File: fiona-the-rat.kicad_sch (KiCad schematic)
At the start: 54 parts, among them J1 XTAL_TP, J14 GND_TP_2, J15 GND_TP_3, J16 USB_TP_N, J17 USB_TP_P, J2 USB_C_Receptacle_PowerOnly_6P, J3 GND_TP_1, J4 VBAT_ADC_TP, J5 ~{CHG}_TP, J6 +1V1_TP, J7 VBAT_TP, J8 +3V3_TP, J9 SWD, SW1 1825027-8, U1 RP2040, U3 W25Q128JVSIQ, U4 BQ21040DBVR, U5 AP2112K-3.3, Y1 Crystal_GND24

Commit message: adding stuff
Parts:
- added J6: Periph, Connector_JST:JST_XH_B2B-XH-A_1x02_P2.50mm_Vertical, symbol Connector:Conn_01x02_Pin
- added MOSFET1: DMN3042L-7, DMN3042L-7-footprints:SOT23_DMN3042L_DIO, symbol 2025-07-08_15-36-45:DMN3042L-7
- added R6: 10K, Resistor_SMD:R_0603_1608Metric, symbol Device:R
- renumbered J17 to J1, J5 to J10, J6 to J11, J7 to J12, J8 to J13, J9 to J14, J16 to J2, J1 to J3, J2 to J4, J4 to J5, J3 to J7, J14 to J8, J15 to J9, R9 to R10, R6 to R7, R7 to R8, R8 to R9
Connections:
- net GND: now also MOSFET1.2 (S), R6.1
- net VBAT: now also J6.2 (Pin_2)
- net LEDs/DIN: now reaches U1.5 (GPIO3)
- net at U1.6 (GPIO4): now also MOSFET1.1 (G), R6.2
- new net: J6.1 (Pin_1), MOSFET1.3 (D)
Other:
- added sheet LEDs (LEDs.kicad_sch)

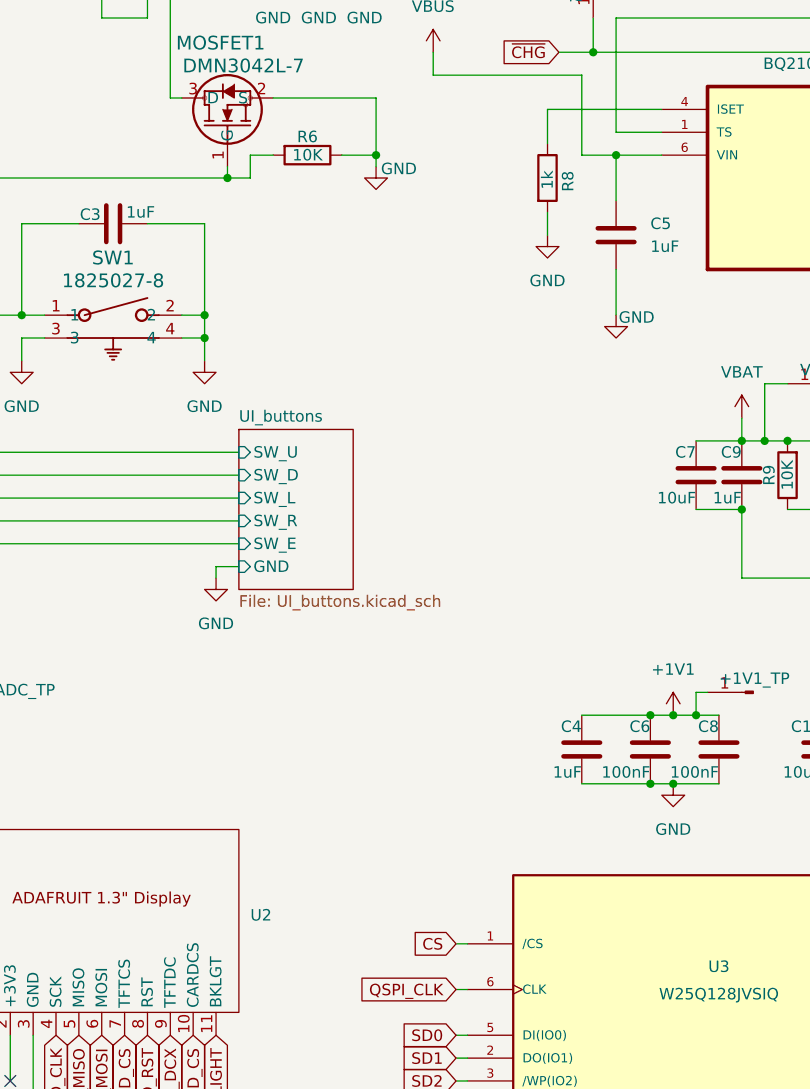
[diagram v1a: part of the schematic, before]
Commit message: changed lib to owned
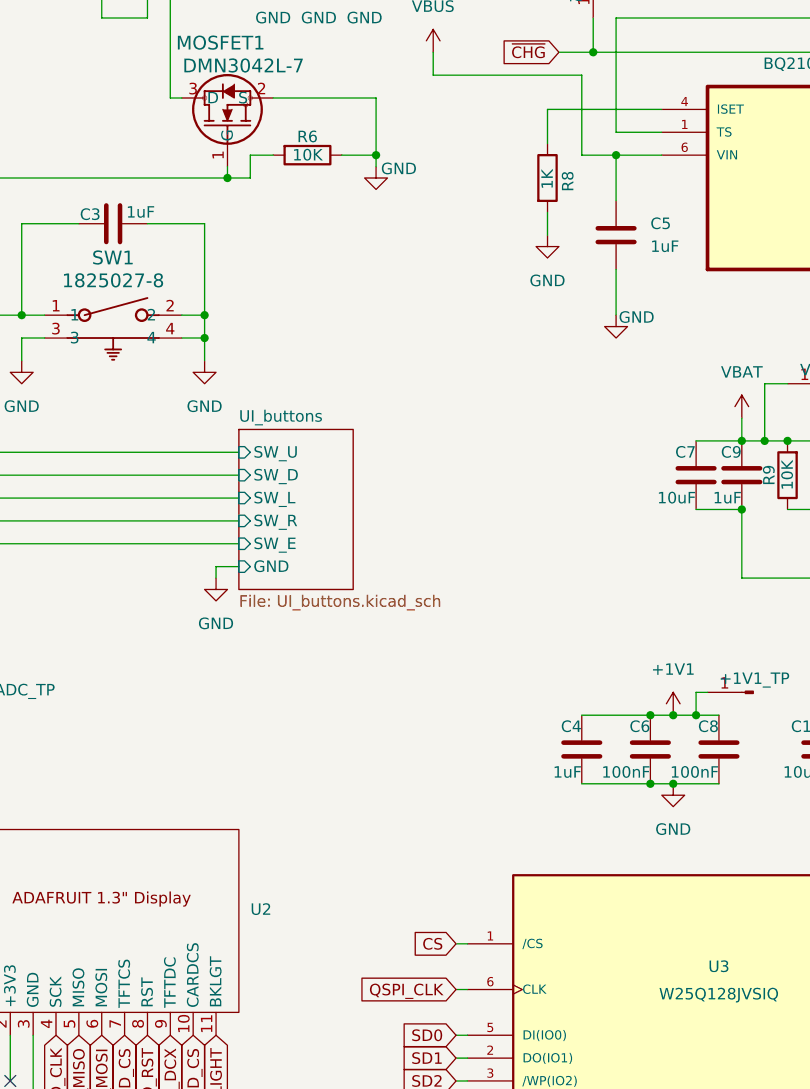
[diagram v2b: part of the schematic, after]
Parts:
- MOSFET1: footprint DMN3042L-7-footprints:SOT23_DMN3042L_DIO -> pfornage-kicad-lib:SOT23_DMN3042L_DIO; symbol 2025-07-08_15-36-45:DMN3042L-7 -> pfornage-kicad-lib:DMN3042L-7
- R8: value 1k -> 1K
- SW1: footprint 1825027_8:SW2_1825027-C_TEC -> pfornage-kicad-lib:SW2_1825027-C_TEC; symbol 1825027_8:1825027-8 -> pfornage-kicad-lib:1825027-8
- U2: footprint Adafruit-1.3-inch-display:display -> pfornage-kicad-lib:adafruit-4313-display; symbol Adafruit-1.3-inch-display:display -> pfornage-kicad-lib:adafruit-4313-display
- U3: footprint W25Q128JVSIQ:SOIC127P790X216-8N -> pfornage-kicad-lib:SOIC127P790X216-8N; symbol W25Q128JVSIQ:W25Q128JVSIQ -> pfornage-kicad-lib:W25Q128JVSIQ
- U4: footprint BQ21040DBVR:SOT95P280X145-6N -> pfornage-kicad-lib:SOT95P280X145-6N; symbol BQ21040DBVR:BQ21040DBVR -> pfornage-kicad-lib:BQ21040DBVR
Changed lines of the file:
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@@
 	)
 	(symbol
-		(lib_id "W25Q128JVSIQ:W25Q128JVSIQ")
+		(lib_id "pfornage-kicad-lib:W25Q128JVSIQ")
 		(at 186.69 139.7 0)
 		(unit 1)
@@
 			)
 		)
-		(property "Footprint" "W25Q128JVSIQ:SOIC127P790X216-8N"
+		(property "Footprint" "pfornage-kicad-lib:SOIC127P790X216-8N"
 			(at 186.69 139.7 0)
 			(effects
@@
 	)
 	(symbol
-		(lib_id "BQ21040DBVR:BQ21040DBVR")
+		(lib_id "pfornage-kicad-lib:BQ21040DBVR")
 		(at 198.12 46.99 0)
 		(unit 1)
@@
 			)
 		)
-		(property "Footprint" "BQ21040DBVR:SOT95P280X145-6N"
+		(property "Footprint" "pfornage-kicad-lib:SOT95P280X145-6N"
 			(at 198.12 46.99 0)
 			(effects
@@
 			)
 		)
-		(property "Value" "1k"
+		(property "Value" "1K"
 			(at 167.64 48.2599 90)
 			(effects
@@
 	)
 	(symbol
-		(lib_id "2025-07-08_15-36-45:DMN3042L-7")
+		(lib_id "pfornage-kicad-lib:DMN3042L-7")
 		(at 132.08 45.72 90)
 		(unit 1)
@@
 			)
 		)
-		(property "Footprint" "DMN3042L-7-footprints:SOT23_DMN3042L_DIO"
+		(property "Footprint" "pfornage-kicad-lib:SOT23_DMN3042L_DIO"
 			(at 132.08 45.72 0)
 			(effects
@@
 	)
 	(symbol
-		(lib_id "Adafruit-1.3-inch-display:display")
+		(lib_id "pfornage-kicad-lib:adafruit-4313-display")
 		(at 118.11 127 0)
 		(unit 1)
@@
 		(fields_autoplaced yes)
 		(property "Reference" "U2"
-			(at 134.62 128.9049 0)
+			(at 134.62 128.2699 0)
 			(effects
 				(font
@@
 		)
 		(property "Value" "~"
-			(at 134.62 130.81 0)
+			(at 134.62 130.8099 0)
 			(effects
 				(font
@@
 				)
 				(justify left)
+				(hide yes)
 			)
 		)
-		(property "Footprint" "Adafruit-1.3-inch-display:display"
+		(property "Footprint" "pfornage-kicad-lib:adafruit-4313-display"
 			(at 118.618 122.174 0)
 			(effects
@@
 	)
 	(symbol
-		(lib_id "1825027_8:1825027-8")
+		(lib_id "pfornage-kicad-lib:1825027-8")
 		(at 111.76 62.23 0)
 		(unit 1)
@@
 			)
 		)
-		(property "Footprint" "1825027_8:SW2_1825027-C_TEC"
+		(property "Footprint" "pfornage-kicad-lib:SW2_1825027-C_TEC"
 			(at 111.76 62.23 0)
 			(effects

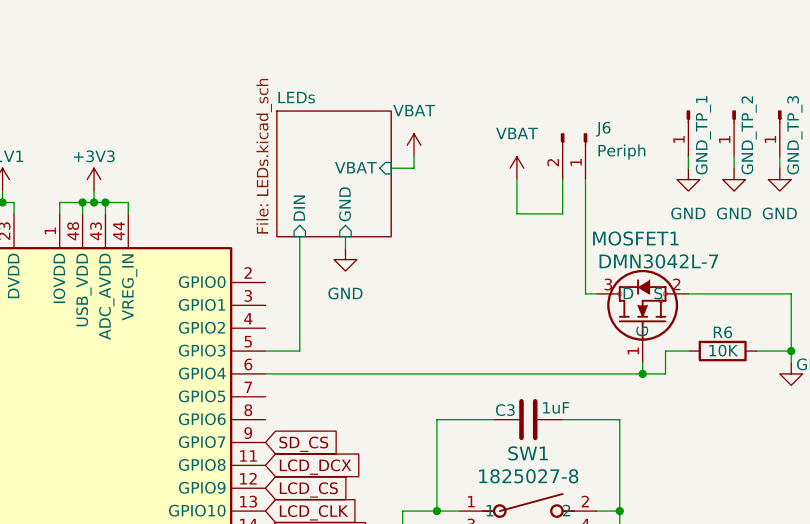
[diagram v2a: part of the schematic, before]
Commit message: breakout GPIO[0..=2]
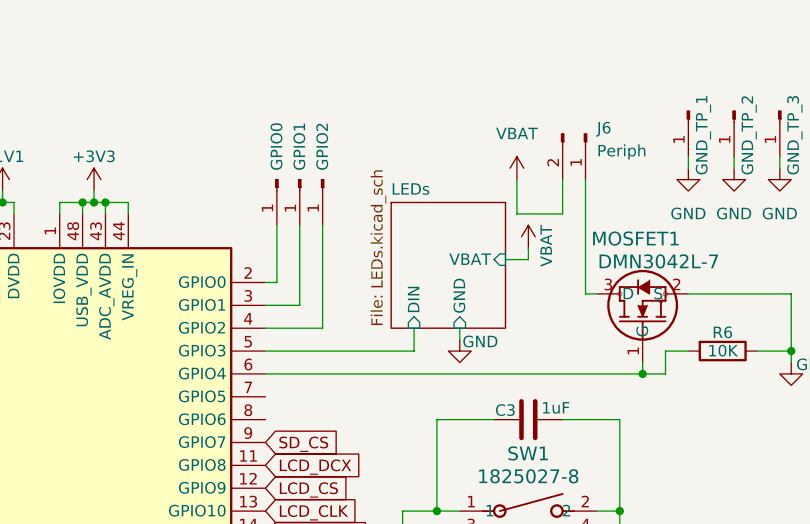
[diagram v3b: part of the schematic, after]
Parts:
- added J19: GPIO0, Connector_PinHeader_2.54mm:PinHeader_1x01_P2.54mm_Vertical, symbol Connector:Conn_01x01_Pin
- added J20: GPIO1, Connector_PinHeader_2.54mm:PinHeader_1x01_P2.54mm_Vertical, symbol Connector:Conn_01x01_Pin
- added J21: GPIO2, Connector_PinHeader_2.54mm:PinHeader_1x01_P2.54mm_Vertical, symbol Connector:Conn_01x01_Pin
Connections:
- net at U1.2 (GPIO0): now also J19.1 (Pin_1)
- net at U1.3 (GPIO1): now also J20.1 (Pin_1)
- net at U1.4 (GPIO2): now also J21.1 (Pin_1)

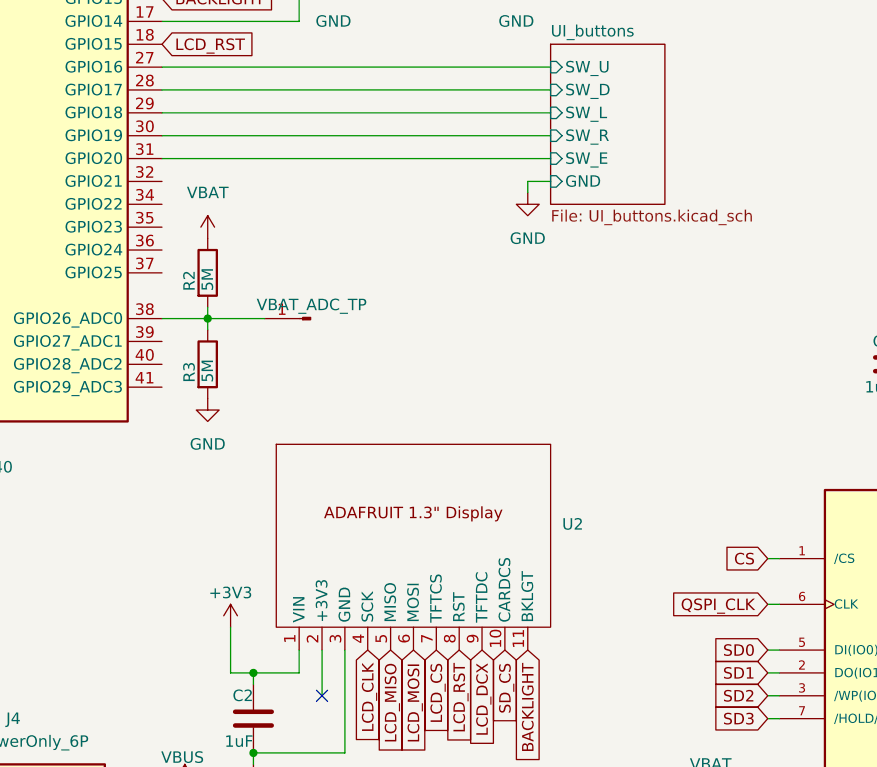
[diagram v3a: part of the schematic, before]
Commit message: add haptic motor
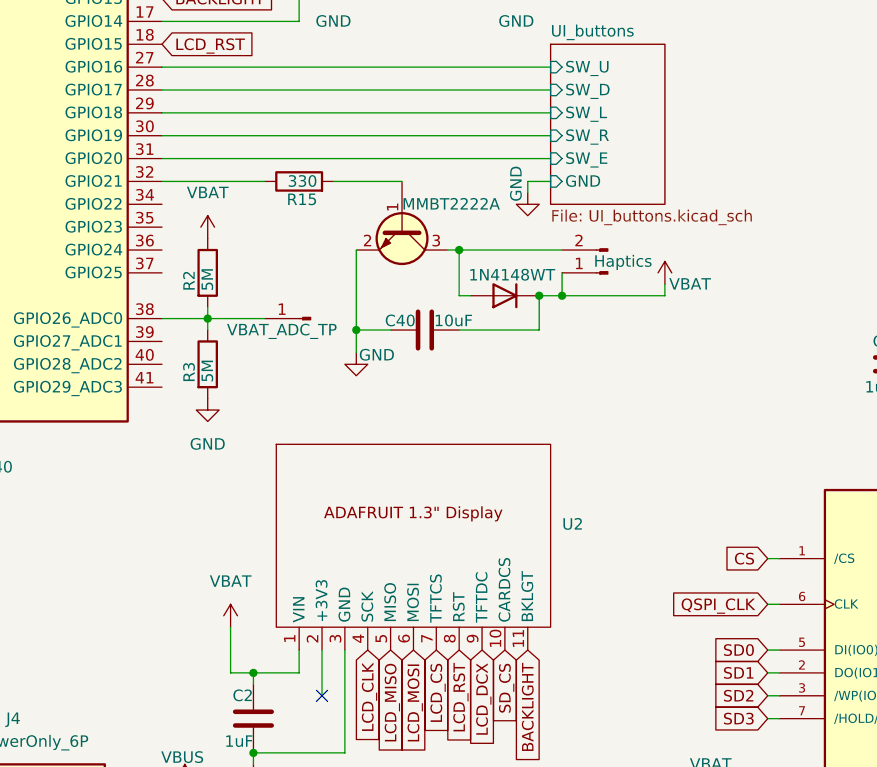
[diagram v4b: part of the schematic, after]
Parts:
- added C40: 10uF, Capacitor_SMD:C_0603_1608Metric, symbol Device:C
- added D2: 1N4148WT, Diode_SMD:D_SOD-523, symbol Diode:1N4148WT
- added J22: Haptics, Connector_JST:JST_XH_B2B-XH-A_1x02_P2.50mm_Vertical, symbol Connector:Conn_01x02_Pin
- added Q1: MMBT2222A, PCM_Package_TO_SOT_SMD_AKL:SOT-23, symbol PCM_Transistor_BJT_AKL:MMBT2222A
- added R15: 330, Resistor_SMD:R_0603_1608Metric, symbol Device:R
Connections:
- net +3V3: no longer C2.1, U2.1 (VIN)
- net GND: now also C40.1, Q1.2 (E)
- net VBAT: now also C2.1, U2.1 (VIN), C40.2, D2.1 (K), J22.1 (Pin_1)
- net at U1.32 (GPIO21): now also R15.1
- new net: Q1.1 (B), R15.2
- new net: D2.2 (A), J22.2 (Pin_2), Q1.3 (C)

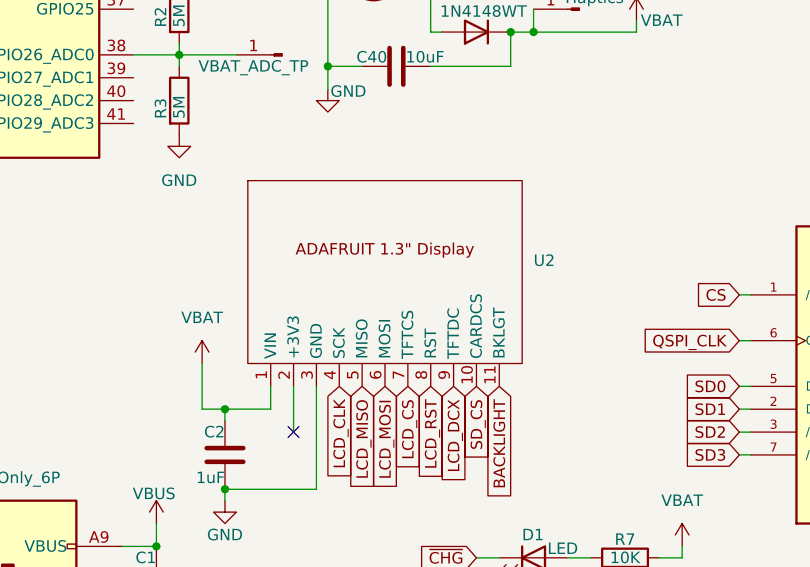
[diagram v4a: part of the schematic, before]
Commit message: Flipped display pin ordering
:/
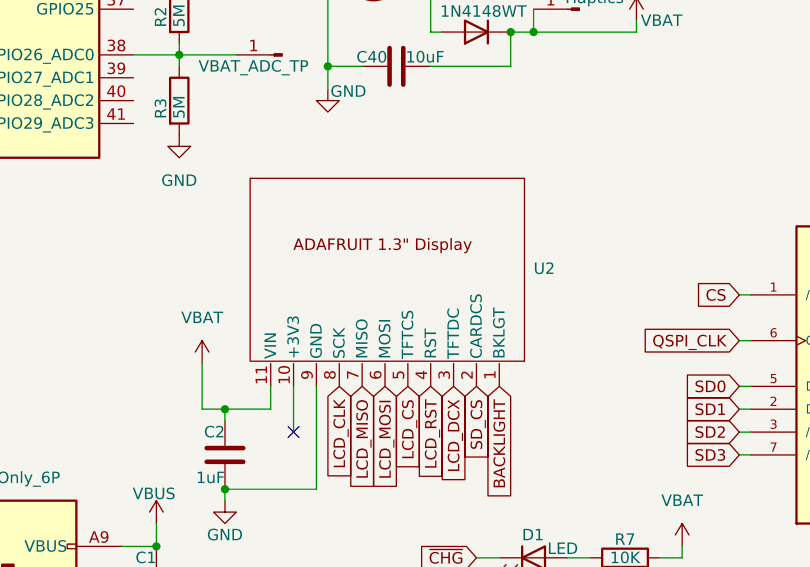
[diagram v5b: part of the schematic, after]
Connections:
- net BACKLIGHT: now also U2.1 (BKLGT); no longer U2.11 (BKLGT)
- net GND: now also U2.9 (GND); no longer U2.3 (GND)
- net LCD_CLK: now also U2.8 (SCK); no longer U2.4 (SCK)
- net LCD_CS: now also U2.5 (TFTCS); no longer U2.7 (TFTCS)
- net LCD_DCX: now also U2.3 (TFTDC); no longer U2.9 (TFTDC)
- net LCD_MISO: now also U2.7 (MISO); no longer U2.5 (MISO)
- net LCD_RST: now also U2.4 (RST); no longer U2.8 (RST)
- net SD_CS: now also U2.2 (CARDCS); no longer U2.10 (CARDCS)
- net VBAT: now also U2.11 (VIN); no longer U2.1 (VIN)
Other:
- moved on the sheet: U2
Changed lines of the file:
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@@
 	(symbol
 		(lib_id "pfornage-kicad-lib:adafruit-4313-display")
-		(at 118.11 127 0)
+		(at 118.11 134.62 180)
 		(unit 1)
 		(exclude_from_sim no)
@@
 		(fields_autoplaced yes)
 		(property "Reference" "U2"
-			(at 134.62 128.2699 0)
+			(at 134.62 129.1589 0)
 			(effects
 				(font
 					(size 1.27 1.27)
 				)
-				(justify left)
+				(justify right)
 			)
 		)
 		(property "Value" "~"
-			(at 134.62 130.8099 0)
+			(at 101.6 130.8101 0)
 			(effects
 				(font
@@
 		)
 		(property "Footprint" "pfornage-kicad-lib:adafruit-4313-display"
-			(at 118.618 122.174 0)
+			(at 117.602 139.446 0)
 			(effects
 				(font
@@
 		)
 		(property "Datasheet" ""
-			(at 118.11 127 0)
+			(at 118.11 134.62 0)
 			(effects
 				(font
@@
 		)
 		(property "Description" ""
-			(at 118.11 127 0)
+			(at 118.11 134.62 0)
 			(effects
 				(font

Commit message: swap crystal lib
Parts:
- removed Y1: Crystal_GND24, Crystal:Crystal_SMD_Abracon_ABM8G-4Pin_3.2x2.5mm, symbol Device:Crystal_GND24
- added Y2: ABM8G-12.000MHZ-18-D2Y-T, pfornage-kicad-lib:XTAL_ABM8G-12.000MHZ-18-D2Y-T, symbol pfornage-kicad-lib:ABM8G-12.000MHZ-18-D2Y-T
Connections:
- net GND: now also Y2.2 (GND), Y2.4 (GND)
- net XTAL_IN: now also Y2.3
- net XTAL_O: now also Y2.1
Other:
- moved on the sheet: C20, R10
